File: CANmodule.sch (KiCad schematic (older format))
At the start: 15 parts, among them U3 TLP2361, U4 TLP2361, U5 MCP2551-I/SN

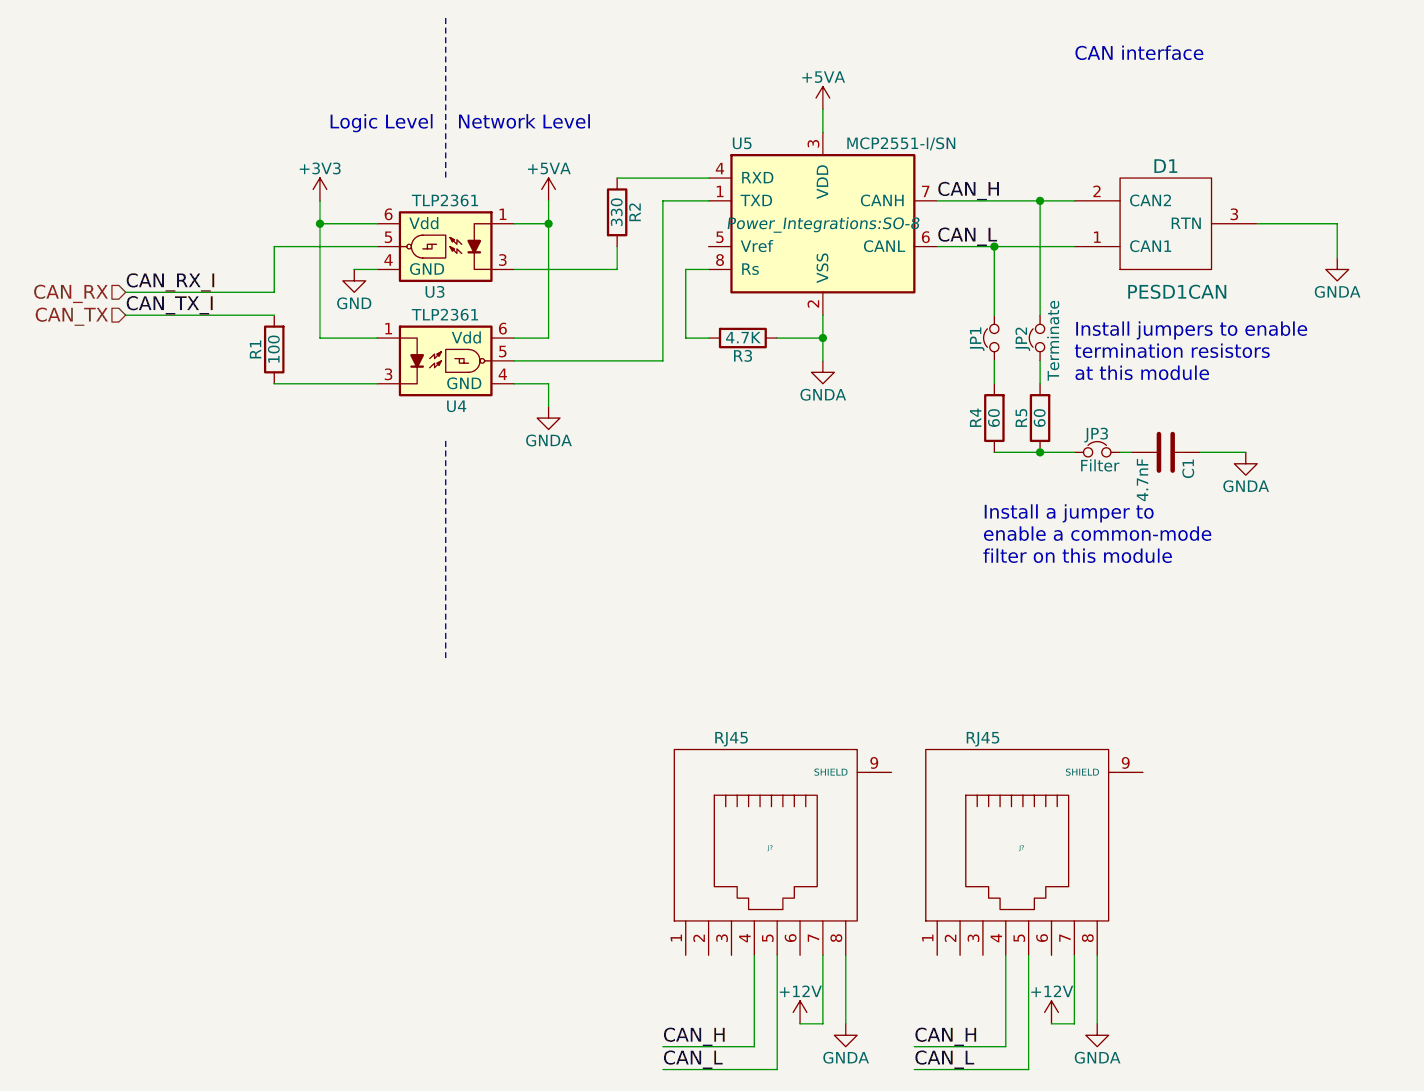
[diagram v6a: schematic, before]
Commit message: most associations, started pcb
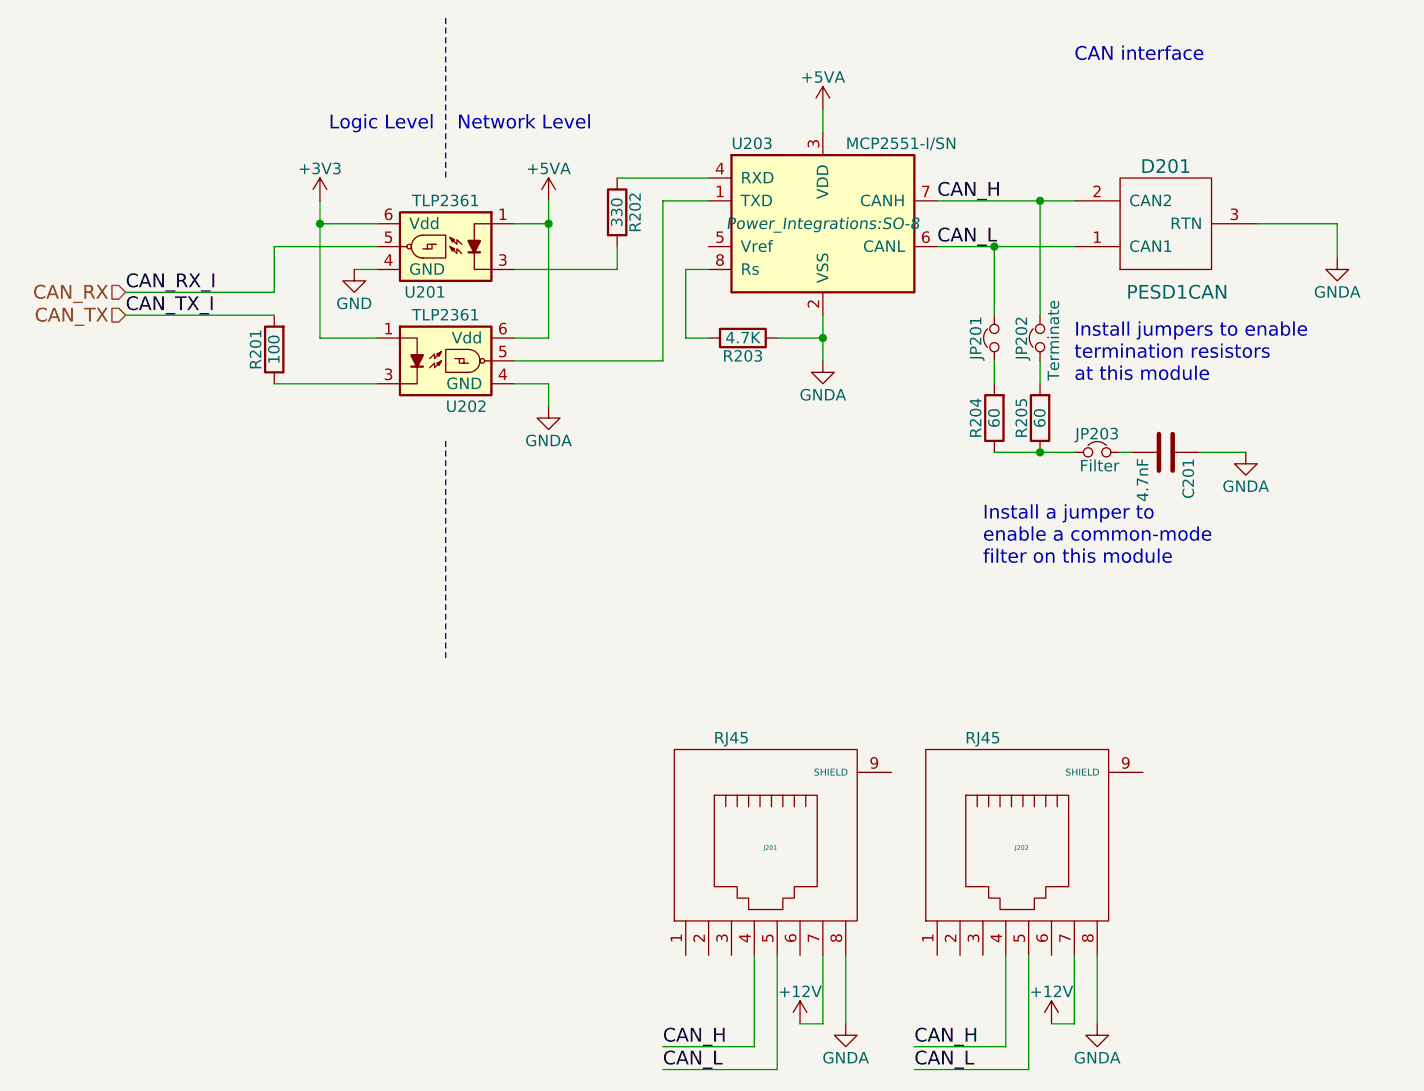
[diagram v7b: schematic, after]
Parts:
- C201: renamed from C1; footprint Capacitors_SMD:C_1206 -> Capacitors_SMD:C_1210_HandSoldering
- R201: renamed from R1; footprint Resistors_SMD:R_1210_HandSoldering -> Resistors_SMD:R_1206_HandSoldering
- R202: renamed from R2; footprint Resistors_SMD:R_1210_HandSoldering -> Resistors_SMD:R_1206_HandSoldering
- R203: renamed from R3; footprint Resistors_SMD:R_1210_HandSoldering -> Resistors_SMD:R_1206_HandSoldering
- gave numbers to parts that had none: 2
- renumbered D1 to D201, JP1 to JP201, JP2 to JP202, JP3 to JP203, R4 to R204, R5 to R205, U3 to U201, U4 to U202, U5 to U203
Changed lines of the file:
@@
 $EndDescr
 $Comp
-L R R3
+L R R203
 U 1 1 57FCAEE8
 P 6850 2000
-F 0 "R3" V 6930 2000 50  0000 C CNN
+F 0 "R203" V 6930 2000 50  0000 C CNN
 F 1 "4.7K" V 6850 2000 50  0000 C CNN
-F 2 "Resistors_SMD:R_1210_HandSoldering" V 6780 2000 50  0001 C CNN
+F 2 "Resistors_SMD:R_1206_HandSoldering" V 6780 2000 50  0001 C CNN
 F 3 "" H 6850 2000 50  0000 C CNN
 	1    6850 2000
@@
 $EndComp
 $Comp
-L C C1
+L C C201
 U 1 1 57FCAEE9
 P 8700 2500
-F 0 "C1" H 8725 2600 50  0000 L CNN
+F 0 "C201" H 8725 2600 50  0000 L CNN
 F 1 "4.7nF" H 8725 2400 50  0000 L CNN
-F 2 "Capacitors_SMD:C_1206" H 8738 2350 50  0001 C CNN
+F 2 "Capacitors_SMD:C_1210_HandSoldering" H 8738 2350 50  0001 C CNN
 F 3 "" H 8700 2500 50  0000 C CNN
 	1    8700 2500
@@
 $EndComp
 $Comp
-L R R4
+L R R204
 U 1 1 57FCAEEA
 P 7950 2350
-F 0 "R4" V 8030 2350 50  0000 C CNN
+F 0 "R204" V 8030 2350 50  0000 C CNN
 F 1 "60" V 7950 2350 50  0000 C CNN
 F 2 "Resistors_SMD:R_1210_HandSoldering" V 7880 2350 50  0001 C CNN
@@
 $EndComp
 $Comp
-L R R5
+L R R205
 U 1 1 57FCAEEB
 P 8150 2350
-F 0 "R5" V 8230 2350 50  0000 C CNN
+F 0 "R205" V 8230 2350 50  0000 C CNN
 F 1 "60" V 8150 2350 50  0000 C CNN
 F 2 "Resistors_SMD:R_1210_HandSoldering" V 8080 2350 50  0001 C CNN
@@
 CAN_L
 $Comp
-L R R2
+L R R202
 U 1 1 57FCAEF2
 P 6300 1450
-F 0 "R2" V 6380 1450 50  0000 C CNN
+F 0 "R202" V 6380 1450 50  0000 C CNN
 F 1 "330" V 6300 1450 50  0000 C CNN
-F 2 "Resistors_SMD:R_1210_HandSoldering" V 6230 1450 50  0001 C CNN
+F 2 "Resistors_SMD:R_1206_HandSoldering" V 6230 1450 50  0001 C CNN
 F 3 "" H 6300 1450 50  0000 C CNN
 	1    6300 1450
@@
 $EndComp
 $Comp
-L Jumper_NC_Small JP1
+L Jumper_NC_Small JP201
 U 1 1 57FCAEF3
 P 7950 2000
-F 0 "JP1" H 7950 2080 50  0000 C CNN
+F 0 "JP201" H 7950 2080 50  0000 C CNN
 F 1 "Terminate" H 7960 1940 50  0001 C CNN
 F 2 "electric_car_lib:JumperSingle" H 7950 2000 50  0001 C CNN
@@
 $EndComp
 $Comp
-L Jumper_NC_Small JP2
+L Jumper_NC_Small JP202
 U 1 1 57FCAEF4
 P 8150 2000
-F 0 "JP2" H 8150 2080 50  0000 C CNN
+F 0 "JP202" H 8150 2080 50  0000 C CNN
 F 1 "Terminate" H 8160 1940 50  0000 C CNN
 F 2 "electric_car_lib:JumperSingle" H 8150 2000 50  0001 C CNN
@@
 $EndComp
 $Comp
-L Jumper_NC_Small JP3
+L Jumper_NC_Small JP203
 U 1 1 57FCAEF5
 P 8400 2500
-F 0 "JP3" H 8400 2580 50  0000 C CNN
+F 0 "JP203" H 8400 2580 50  0000 C CNN
 F 1 "Filter" H 8410 2440 50  0000 C CNN
 F 2 "electric_car_lib:JumperSingle" H 8400 2500 50  0001 C CNN
@@
 $EndComp
 $Comp
-L R R1
+L R R201
 U 1 1 57FCAEF6
 P 4800 2050
-F 0 "R1" V 4880 2050 50  0000 C CNN
+F 0 "R201" V 4880 2050 50  0000 C CNN
 F 1 "100" V 4800 2050 50  0000 C CNN
-F 2 "Resistors_SMD:R_1210_HandSoldering" V 4730 2050 50  0001 C CNN
+F 2 "Resistors_SMD:R_1206_HandSoldering" V 4730 2050 50  0001 C CNN
 F 3 "" H 4800 2050 50  0000 C CNN
 	1    4800 2050
@@
 $EndComp
 $Comp
-L GND #PWR013
+L GND #PWR032
 U 1 1 57FCAEF7
 P 5150 1700
-F 0 "#PWR013" H 5150 1450 50  0001 C CNN
+F 0 "#PWR032" H 5150 1450 50  0001 C CNN
 F 1 "GND" H 5150 1550 50  0000 C CNN
 F 2 "" H 5150 1700 50  0000 C CNN
@@
 $EndComp
 $Comp
-L TLP2361 U4
+L TLP2361 U202
 U 1 1 57FCAEF8
 P 5550 2100
-F 0 "U4" H 5550 1900 50  0000 L CNN
+F 0 "U202" H 5550 1900 50  0000 L CNN
 F 1 "TLP2361" H 5550 2300 50  0000 C CNN
 F 2 "electric_car_lib:soic-5" H 5350 1900 50  0001 L CIN
@@
 $EndComp
 $Comp
-L TLP2361 U3
+L TLP2361 U201
 U 1 1 57FCAEF9
 P 5550 1600
-F 0 "U3" H 5550 1400 50  0000 L CNN
+F 0 "U201" H 5550 1400 50  0000 L CNN
 F 1 "TLP2361" H 5550 1800 50  0000 C CNN
 F 2 "electric_car_lib:soic-5" H 5350 1400 50  0001 L CIN
@@
 CAN interface
 $Comp
-L PESD1CAN D1
+L PESD1CAN D201
 U 1 1 57FCAEFA
 P 8700 1500
-F 0 "D1" H 8700 1250 60  0000 C CNN
+F 0 "D201" H 8700 1250 60  0000 C CNN
 F 1 "PESD1CAN" H 8650 1800 60  0000 C CNN
 F 2 "TO_SOT_Packages_SMD:SOT-23_Handsoldering" H 8700 1500 60  0001 C CNN
@@
 $EndComp
 $Comp
-L MCP2551-I/SN U5
+L MCP2551-I/SN U203
 U 1 1 57FCAEFB
 P 7200 1500
-F 0 "U5" H 6800 1850 50  0000 L CNN
+F 0 "U203" H 6800 1850 50  0000 L CNN
 F 1 "MCP2551-I/SN" H 7300 1850 50  0000 L CNN
 F 2 "Power_Integrations:SO-8" H 7200 1500 50  0000 C CIN
@@
 	7000 2000 7200 2000
 Wire Wire Line
-	7200 1900 7200 2000
-Wire Wire Line
-	7200 2000 7200 2100
+	7200 1900 7200 2100
 Connection ~ 7200 2000
 Wire Wire Line
-	7700 1600 7950 1600
-Wire Wire Line
-	7950 1600 8300 1600
-Wire Wire Line
-	7700 1400 8150 1400
-Wire Wire Line
-	8150 1400 8300 1400
+	7700 1600 8300 1600
+Wire Wire Line
+	7700 1400 8300 1400
 Connection ~ 7950 1600
 Connection ~ 8150 1400
@@
 	4800 1600 5250 1600
 Wire Wire Line
-	5000 1400 5000 1500
-Wire Wire Line
-	5000 1500 5000 2000
+	5000 1400 5000 2000
 Wire Wire Line
 	5850 1500 6000 1500
 Wire Wire Line
-	6000 1400 6000 1500
-Wire Wire Line
-	6000 1500 6000 2000
+	6000 1400 6000 2000
 Wire Wire Line
 	7200 1000 7200 1100
@@
 	8150 2100 8150 2200
 Wire Wire Line
-	7950 2500 8150 2500
-Wire Wire Line
-	8150 2500 8300 2500
+	7950 2500 8300 2500
 Wire Wire Line
 	4150 1800 4800 1800
@@
 CAN_L
 $Comp
-L +5VA #PWR?
+L +5VA #PWR033
 U 1 1 582A8343
 P 6000 1400
-F 0 "#PWR?" H 6000 1250 50  0001 C CNN
+F 0 "#PWR033" H 6000 1250 50  0001 C CNN
 F 1 "+5VA" H 6000 1540 50  0000 C CNN
 F 2 "" H 6000 1400 50  0000 C CNN
@@
 $EndComp
 $Comp
-L +5VA #PWR?
+L +5VA #PWR034
 U 1 1 582A84BF
 P 7200 1000
-F 0 "#PWR?" H 7200 850 50  0001 C CNN
+F 0 "#PWR034" H 7200 850 50  0001 C CNN
 F 1 "+5VA" H 7200 1140 50  0000 C CNN
 F 2 "" H 7200 1000 50  0000 C CNN
@@
 $EndComp
 $Comp
-L GNDA #PWR?
+L GNDA #PWR035
 U 1 1 582A8520
 P 6000 2300
-F 0 "#PWR?" H 6000 2050 50  0001 C CNN
+F 0 "#PWR035" H 6000 2050 50  0001 C CNN
 F 1 "GNDA" H 6000 2150 50  0000 C CNN
 F 2 "" H 6000 2300 50  0000 C CNN
@@
 $EndComp
 $Comp
-L GNDA #PWR?
+L GNDA #PWR036
 U 1 1 582A8593
 P 7200 2100
-F 0 "#PWR?" H 7200 1850 50  0001 C CNN
+F 0 "#PWR036" H 7200 1850 50  0001 C CNN
 F 1 "GNDA" H 7200 1950 50  0000 C CNN
 F 2 "" H 7200 2100 50  0000 C CNN
@@
 $EndComp
 $Comp
-L GNDA #PWR?
+L GNDA #PWR037
 U 1 1 582A864A
 P 9450 1650
-F 0 "#PWR?" H 9450 1400 50  0001 C CNN
+F 0 "#PWR037" H 9450 1400 50  0001 C CNN
 F 1 "GNDA" H 9450 1500 50  0000 C CNN
 F 2 "" H 9450 1650 50  0000 C CNN
@@
 $EndComp
 $Comp
-L GNDA #PWR?
+L GNDA #PWR038
 U 1 1 582A86D1
 P 9050 2500
-F 0 "#PWR?" H 9050 2250 50  0001 C CNN
+F 0 "#PWR038" H 9050 2250 50  0001 C CNN
 F 1 "GNDA" H 9050 2350 50  0000 C CNN
 F 2 "" H 9050 2500 50  0000 C CNN
@@
 $EndComp
 $Comp
-L +3V3 #PWR?
+L +3V3 #PWR039
 U 1 1 582A8930
 P 5000 1400
-F 0 "#PWR?" H 5000 1250 50  0001 C CNN
+F 0 "#PWR039" H 5000 1250 50  0001 C CNN
 F 1 "+3V3" H 5000 1540 50  0000 C CNN
 F 2 "" H 5000 1400 50  0000 C CNN
@@
 $EndComp
 $Comp
-L RJ45 J?
+L RJ45 J202
 U 1 1 582DA582
 P 8050 4250
-F 0 "J?" H 8070 4270 20  0000 C CNN
+F 0 "J202" H 8070 4270 20  0000 C CNN
 F 1 "RJ45" H 7900 4750 50  0000 C CNN
 F 2 "Connect:RJ45_8" H 8050 4250 50  0001 C CNN
@@
 $EndComp
 $Comp
-L +12V #PWR?
+L +12V #PWR040
 U 1 1 582DA73C
 P 8200 5000
-F 0 "#PWR?" H 8200 4850 50  0001 C CNN
+F 0 "#PWR040" H 8200 4850 50  0001 C CNN
 F 1 "+12V" H 8200 5140 50  0000 C CNN
 F 2 "" H 8200 5000 50  0000 C CNN
@@
 $EndComp
 $Comp
-L GNDA #PWR?
+L GNDA #PWR041
 U 1 1 582DA7E4
 P 8400 5000
-F 0 "#PWR?" H 8400 4750 50  0001 C CNN
+F 0 "#PWR041" H 8400 4750 50  0001 C CNN
 F 1 "GNDA" H 8400 4850 50  0000 C CNN
 F 2 "" H 8400 5000 50  0000 C CNN
@@
 CAN_L
 $Comp
-L RJ45 J?
+L RJ45 J201
 U 1 1 582DC5CA
 P 6950 4250
-F 0 "J?" H 6970 4270 20  0000 C CNN
+F 0 "J201" H 6970 4270 20  0000 C CNN
 F 1 "RJ45" H 6800 4750 50  0000 C CNN
 F 2 "Connect:RJ45_8" H 6950 4250 50  0001 C CNN
@@
 $EndComp
 $Comp
-L +12V #PWR?
+L +12V #PWR042
 U 1 1 582DC5D0
 P 7100 5000
-F 0 "#PWR?" H 7100 4850 50  0001 C CNN
+F 0 "#PWR042" H 7100 4850 50  0001 C CNN
 F 1 "+12V" H 7100 5140 50  0000 C CNN
 F 2 "" H 7100 5000 50  0000 C CNN
@@
 $EndComp
 $Comp
-L GNDA #PWR?
+L GNDA #PWR043
 U 1 1 582DC5D6
 P 7300 5000
-F 0 "#PWR?" H 7300 4750 50  0001 C CNN
+F 0 "#PWR043" H 7300 4750 50  0001 C CNN
 F 1 "GNDA" H 7300 4850 50  0000 C CNN
 F 2 "" H 7300 5000 50  0000 C CNN

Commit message: minor tweaks, started layout
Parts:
- added R206: 100, Resistors_SMD:R_1206_HandSoldering, symbol R
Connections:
- net CAN_RX: now also R206.1; no longer U201.5
- net GNDA: now also JP203.2; no longer C201.1
- net at C201.2: now also R204.1, R205.1; no longer JP203.2
- new net: C201.1, JP203.1
- new net: R206.2, U201.5
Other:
- moved on the sheet: C201, JP203, R201
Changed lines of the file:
@@
 L C C201
 U 1 1 57FCAEE9
-P 8700 2500
-F 0 "C201" H 8725 2600 50  0000 L CNN
-F 1 "4.7nF" H 8725 2400 50  0000 L CNN
-F 2 "Capacitors_SMD:C_1210_HandSoldering" H 8738 2350 50  0001 C CNN
-F 3 "" H 8700 2500 50  0000 C CNN
-	1    8700 2500
+P 8450 2500
+F 0 "C201" H 8475 2600 50  0000 L CNN
+F 1 "4.7nF" H 8475 2400 50  0000 L CNN
+F 2 "Capacitors_SMD:C_1210_HandSoldering" H 8488 2350 50  0001 C CNN
+F 3 "" H 8450 2500 50  0000 C CNN
+	1    8450 2500
 	0    1    1    0
 $EndComp
@@
 L Jumper_NC_Small JP203
 U 1 1 57FCAEF5
-P 8400 2500
-F 0 "JP203" H 8400 2580 50  0000 C CNN
-F 1 "Filter" H 8410 2440 50  0000 C CNN
-F 2 "electric_car_lib:JumperSingle" H 8400 2500 50  0001 C CNN
-F 3 "" H 8400 2500 50  0000 C CNN
-	1    8400 2500
+P 8750 2500
+F 0 "JP203" H 8750 2580 50  0000 C CNN
+F 1 "Filter" H 8760 2440 50  0000 C CNN
+F 2 "electric_car_lib:JumperSingle" H 8750 2500 50  0001 C CNN
+F 3 "" H 8750 2500 50  0000 C CNN
+	1    8750 2500
 	1    0    0    -1
 $EndComp
@@
 L R R201
 U 1 1 57FCAEF6
-P 4800 2050
-F 0 "R201" V 4880 2050 50  0000 C CNN
-F 1 "100" V 4800 2050 50  0000 C CNN
-F 2 "Resistors_SMD:R_1206_HandSoldering" V 4730 2050 50  0001 C CNN
-F 3 "" H 4800 2050 50  0000 C CNN
-	1    4800 2050
+P 4600 2050
+F 0 "R201" V 4680 2050 50  0000 C CNN
+F 1 "100" V 4600 2050 50  0000 C CNN
+F 2 "Resistors_SMD:R_1206_HandSoldering" V 4530 2050 50  0001 C CNN
+F 3 "" H 4600 2050 50  0000 C CNN
+	1    4600 2050
 	-1   0    0    1
 $EndComp
 $Comp
-L GND #PWR032
+L GND #PWR031
 U 1 1 57FCAEF7
 P 5150 1700
-F 0 "#PWR032" H 5150 1450 50  0001 C CNN
+F 0 "#PWR031" H 5150 1450 50  0001 C CNN
 F 1 "GND" H 5150 1550 50  0000 C CNN
 F 2 "" H 5150 1700 50  0000 C CNN
@@
 	6500 1400 6700 1400
 Wire Wire Line
-	4800 1800 4800 1600
-Wire Wire Line
-	4800 1600 5250 1600
+	4600 1800 4600 1600
 Wire Wire Line
 	5000 1400 5000 2000
@@
 	7950 2500 8300 2500
 Wire Wire Line
-	4150 1800 4800 1800
-Wire Wire Line
-	4800 1900 4150 1900
+	4150 1800 4600 1800
+Wire Wire Line
+	4600 1900 4150 1900
 Wire Wire Line
 	5000 1500 5250 1500
@@
 	5000 2000 5250 2000
 Wire Wire Line
-	5250 2200 4800 2200
+	5250 2200 4600 2200
 Wire Wire Line
 	5250 1700 5150 1700
@@
 	9050 2500 8850 2500
 Wire Wire Line
-	8550 2500 8500 2500
+	8650 2500 8600 2500
 Wire Wire Line
 	9100 1500 9450 1500
@@
 CAN_L
 $Comp
-L +5VA #PWR033
+L +5VA #PWR032
 U 1 1 582A8343
 P 6000 1400
-F 0 "#PWR033" H 6000 1250 50  0001 C CNN
+F 0 "#PWR032" H 6000 1250 50  0001 C CNN
 F 1 "+5VA" H 6000 1540 50  0000 C CNN
 F 2 "" H 6000 1400 50  0000 C CNN
@@
 $EndComp
 $Comp
-L +5VA #PWR034
+L +5VA #PWR033
 U 1 1 582A84BF
 P 7200 1000
-F 0 "#PWR034" H 7200 850 50  0001 C CNN
+F 0 "#PWR033" H 7200 850 50  0001 C CNN
 F 1 "+5VA" H 7200 1140 50  0000 C CNN
 F 2 "" H 7200 1000 50  0000 C CNN
@@
 $EndComp
 $Comp
-L GNDA #PWR035
+L GNDA #PWR034
 U 1 1 582A8520
 P 6000 2300
-F 0 "#PWR035" H 6000 2050 50  0001 C CNN
+F 0 "#PWR034" H 6000 2050 50  0001 C CNN
 F 1 "GNDA" H 6000 2150 50  0000 C CNN
 F 2 "" H 6000 2300 50  0000 C CNN
@@
 $EndComp
 $Comp
-L GNDA #PWR036
+L GNDA #PWR035
 U 1 1 582A8593
 P 7200 2100
-F 0 "#PWR036" H 7200 1850 50  0001 C CNN
+F 0 "#PWR035" H 7200 1850 50  0001 C CNN
 F 1 "GNDA" H 7200 1950 50  0000 C CNN
 F 2 "" H 7200 2100 50  0000 C CNN
@@
 $EndComp
 $Comp
-L GNDA #PWR037
+L GNDA #PWR036
 U 1 1 582A864A
 P 9450 1650
-F 0 "#PWR037" H 9450 1400 50  0001 C CNN
+F 0 "#PWR036" H 9450 1400 50  0001 C CNN
 F 1 "GNDA" H 9450 1500 50  0000 C CNN
 F 2 "" H 9450 1650 50  0000 C CNN
@@
 $EndComp
 $Comp
-L GNDA #PWR038
+L GNDA #PWR037
 U 1 1 582A86D1
 P 9050 2500
-F 0 "#PWR038" H 9050 2250 50  0001 C CNN
+F 0 "#PWR037" H 9050 2250 50  0001 C CNN
 F 1 "GNDA" H 9050 2350 50  0000 C CNN
 F 2 "" H 9050 2500 50  0000 C CNN
@@
 $EndComp
 $Comp
-L +3V3 #PWR039
+L +3V3 #PWR038
 U 1 1 582A8930
 P 5000 1400
-F 0 "#PWR039" H 5000 1250 50  0001 C CNN
+F 0 "#PWR038" H 5000 1250 50  0001 C CNN
 F 1 "+3V3" H 5000 1540 50  0000 C CNN
 F 2 "" H 5000 1400 50  0000 C CNN
@@
 $EndComp
 $Comp
-L +12V #PWR040
+L +12V #PWR039
 U 1 1 582DA73C
 P 8200 5000
-F 0 "#PWR040" H 8200 4850 50  0001 C CNN
+F 0 "#PWR039" H 8200 4850 50  0001 C CNN
 F 1 "+12V" H 8200 5140 50  0000 C CNN
 F 2 "" H 8200 5000 50  0000 C CNN
@@
 $EndComp
 $Comp
-L GNDA #PWR041
+L GNDA #PWR040
 U 1 1 582DA7E4
 P 8400 5000
-F 0 "#PWR041" H 8400 4750 50  0001 C CNN
+F 0 "#PWR040" H 8400 4750 50  0001 C CNN
 F 1 "GNDA" H 8400 4850 50  0000 C CNN
 F 2 "" H 8400 5000 50  0000 C CNN
@@
 $EndComp
 $Comp
-L +12V #PWR042
+L +12V #PWR041
 U 1 1 582DC5D0
 P 7100 5000
-F 0 "#PWR042" H 7100 4850 50  0001 C CNN
+F 0 "#PWR041" H 7100 4850 50  0001 C CNN
 F 1 "+12V" H 7100 5140 50  0000 C CNN
 F 2 "" H 7100 5000 50  0000 C CNN
@@
 $EndComp
 $Comp
-L GNDA #PWR043
+L GNDA #PWR042
 U 1 1 582DC5D6
 P 7300 5000
-F 0 "#PWR043" H 7300 4750 50  0001 C CNN
+F 0 "#PWR042" H 7300 4750 50  0001 C CNN
 F 1 "GNDA" H 7300 4850 50  0000 C CNN
 F 2 "" H 7300 5000 50  0000 C CNN
@@
 Wire Wire Line
 	7200 5000 7200 4700
+$Comp
+L R R206
+U 1 1 582C478D
+P 4750 1600
+F 0 "R206" V 4830 1600 50  0000 C CNN
+F 1 "100" V 4750 1600 50  0000 C CNN
+F 2 "Resistors_SMD:R_1206_HandSoldering" V 4680 1600 50  0001 C CNN
+F 3 "" H 4750 1600 50  0000 C CNN
+	1    4750 1600
+	0    -1   -1   0
+$EndComp
+Wire Wire Line
+	4900 1600 5250 1600
 $EndSCHEMATC
